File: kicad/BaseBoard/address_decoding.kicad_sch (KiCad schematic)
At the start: 5 parts, among them U5 74LS00, U6 ATF22V10C

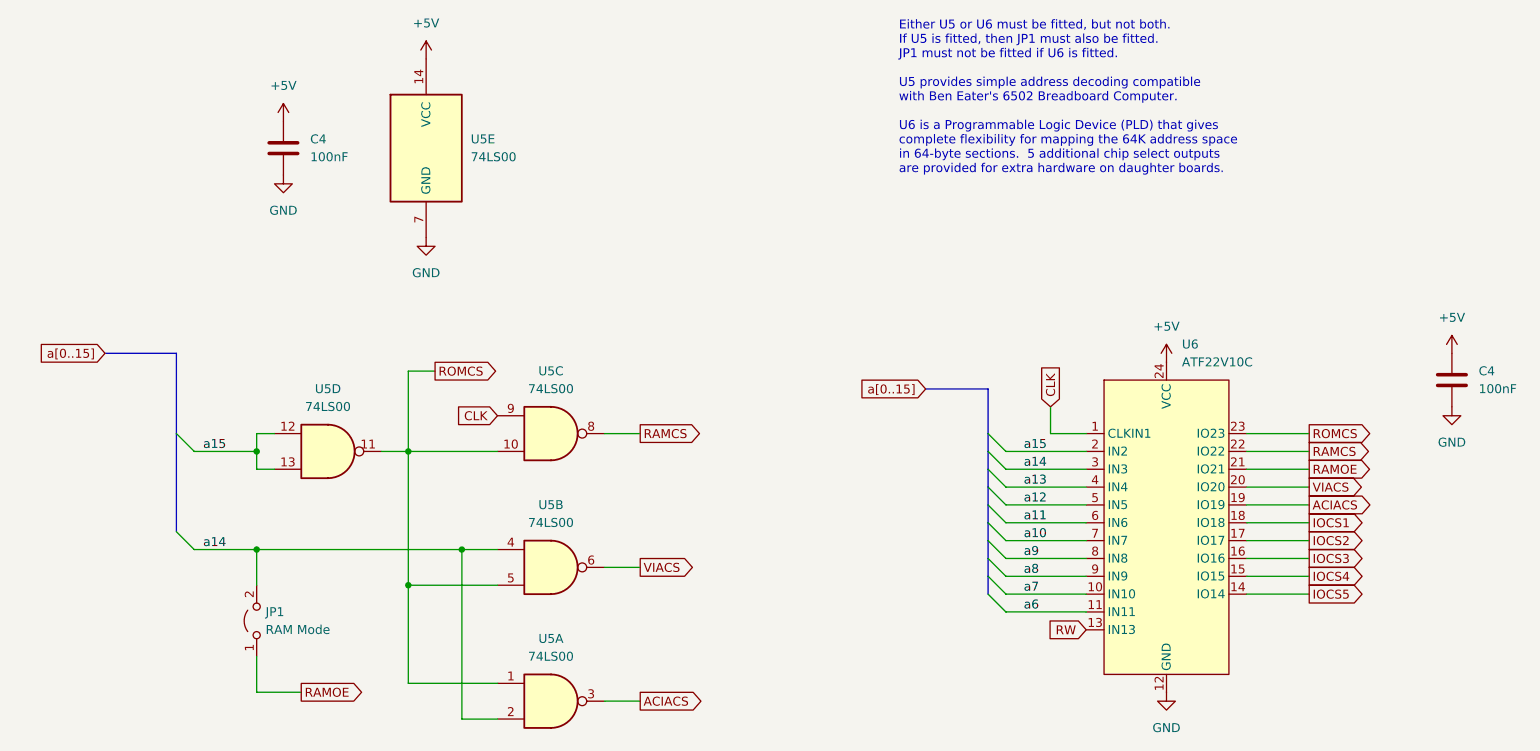
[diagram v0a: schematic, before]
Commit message: I/O board schematic and layout
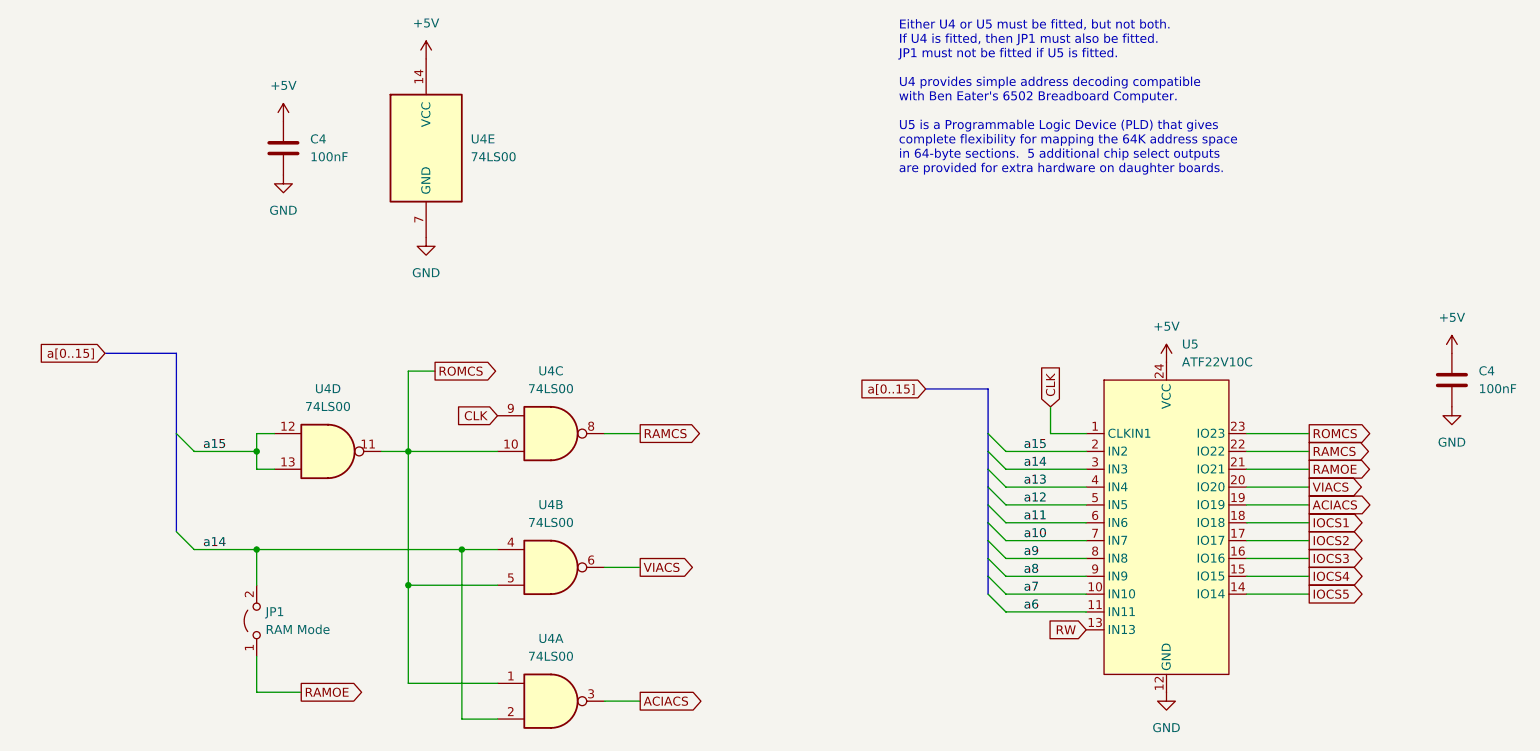
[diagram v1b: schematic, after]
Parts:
- renumbered U5 to U4, U6 to U5
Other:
- note added: "Either U4 or U5 must be fitted, but not both. If U4 is fitted, then JP1 must also be fitted. JP1 must not be fitted if U5 is fitted. U4 provides simple address decoding compatible with Ben Eater's 6502 Breadboard Computer. U5 is a Programmable Logic Device (PLD) that gives complete flexibility for mapping the 64K address space in 64-byte sections. 5 additional chip select outputs are provided for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"
- note removed: "Either U5 or U6 must be fitted, but not both. If U5 is fitted, then JP1 must also be fitted. JP1 must not be fitted if U6 is fitted. U5 provides simple address decoding compatible with Ben Eater's 6502 Breadboard Computer. U6 is a Programmable Logic Device (PLD) that gives complete flexibility for mapping the 64K address space in 64-byte sections. 5 additional chip select outputs are provided for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"
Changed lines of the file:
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@@
     (stroke (width 0) (type default))
   )
-  (text "Either U5 or U6 must be fitted, but not both.\nIf U5 is fitted, then JP1 must also be fitted.\nJP1 must not be fitted if U6 is fitted.\n\nU5 provides simple address decoding compatible\nwith Ben Eater's 6502 Breadboard Computer.\n\nU6 is a Programmable Logic Device (PLD) that gives\ncomplete flexibility for mapping the 64K address space\nin 64-byte sections.  5 additional chip select outputs\nare provided for extra hardware on daughter boards."
+  (text "Either U4 or U5 must be fitted, but not both.\nIf U4 is fitted, then JP1 must also be fitted.\nJP1 must not be fitted if U5 is fitted.\n\nU4 provides simple address decoding compatible\nwith Ben Eater's 6502 Breadboard Computer.\n\nU5 is a Programmable Logic Device (PLD) that gives\ncomplete flexibility for mapping the 64K address space\nin 64-byte sections.  5 additional chip select outputs\nare provided for extra hardware on daughter boards."
     (at 166.37 66.04 0)
     (effects (font (size 1.27 1.27)) (justify left bottom))
@@
         )
         (path "/3f118084-1458-40be-b12b-e8391c9e712b/5996dc94-313e-4b29-a810-4864fe70dd3b"
+          (reference "#PWR034") (unit 1)
+        )
+      )
+    )
+  )
+  (symbol (lib_id "power:GND") (at 99.06 74.93 0) (unit 1)
+    (in_bom yes) (on_board yes) (dnp no) (fields_autoplaced)
+    (property "Reference" "#PWR036" (at 99.06 81.28 0)
+      (effects (font (size 1.27 1.27)) hide)
+    )
+    (property "Value" "GND" (at 99.06 80.01 0)
+      (effects (font (size 1.27 1.27)))
+    )
+    (property "Footprint" "" (at 99.06 74.93 0)
+      (effects (font (size 1.27 1.27)) hide)
+    )
+    (property "Datasheet" "" (at 99.06 74.93 0)
+      (effects (font (size 1.27 1.27)) hide)
+    )
+    (pin "1")
+    (instances
+      (project "MiniComputerBase"
+        (path "/3f118084-1458-40be-b12b-e8391c9e712b/5996dc94-313e-4b29-a810-4864fe70dd3b"
           (reference "#PWR036") (unit 1)
-        )
-      )
-    )
-  )
-  (symbol (lib_id "power:GND") (at 99.06 74.93 0) (unit 1)
-    (in_bom yes) (on_board yes) (dnp no) (fields_autoplaced)
-    (property "Reference" "#PWR038" (at 99.06 81.28 0)
-      (effects (font (size 1.27 1.27)) hide)
-    )
-    (property "Value" "GND" (at 99.06 80.01 0)
-      (effects (font (size 1.27 1.27)))
-    )
-    (property "Footprint" "" (at 99.06 74.93 0)
-      (effects (font (size 1.27 1.27)) hide)
-    )
-    (property "Datasheet" "" (at 99.06 74.93 0)
-      (effects (font (size 1.27 1.27)) hide)
-    )
-    (pin "1")
-    (instances
-      (project "MiniComputerBase"
-        (path "/3f118084-1458-40be-b12b-e8391c9e712b/5996dc94-313e-4b29-a810-4864fe70dd3b"
-          (reference "#PWR038") (unit 1)
         )
       )
@@
   (symbol (lib_id "74xx:74LS00") (at 85.09 105.41 0) (unit 4)
     (in_bom yes) (on_board yes) (dnp no) (fields_autoplaced)
-    (property "Reference" "U5" (at 85.0817 96.52 0)
+    (property "Reference" "U4" (at 85.0817 96.52 0)
       (effects (font (size 1.27 1.27)))
     )
@@
       (project "MiniComputerBase"
         (path "/3f118084-1458-40be-b12b-e8391c9e712b/5996dc94-313e-4b29-a810-4864fe70dd3b"
-          (reference "U5") (unit 4)
+          (reference "U4") (unit 4)
         )
       )
@@
   (symbol (lib_id "74xx:74LS00") (at 116.84 121.92 0) (unit 2)
     (in_bom yes) (on_board yes) (dnp no) (fields_autoplaced)
-    (property "Reference" "U5" (at 116.8317 113.03 0)
+    (property "Reference" "U4" (at 116.8317 113.03 0)
       (effects (font (size 1.27 1.27)))
     )
@@
       (project "MiniComputerBase"
         (path "/3f118084-1458-40be-b12b-e8391c9e712b/5996dc94-313e-4b29-a810-4864fe70dd3b"
-          (reference "U5") (unit 2)
+          (reference "U4") (unit 2)
         )
       )
@@
   (symbol (lib_id "74xx:74LS00") (at 116.84 140.97 0) (unit 1)
     (in_bom yes) (on_board yes) (dnp no) (fields_autoplaced)
-    (property "Reference" "U5" (at 116.8317 132.08 0)
+    (property "Reference" "U4" (at 116.8317 132.08 0)
       (effects (font (size 1.27 1.27)))
     )
@@
       (project "MiniComputerBase"
         (path "/3f118084-1458-40be-b12b-e8391c9e712b/5996dc94-313e-4b29-a810-4864fe70dd3b"
-          (reference "U5") (unit 1)
+          (reference "U4") (unit 1)
         )
       )
@@
   (symbol (lib_id "74xx:74LS00") (at 99.06 62.23 0) (unit 5)
     (in_bom yes) (on_board yes) (dnp no) (fields_autoplaced)
-    (property "Reference" "U5" (at 105.41 60.96 0)
+    (property "Reference" "U4" (at 105.41 60.96 0)
       (effects (font (size 1.27 1.27)) (justify left))
     )
@@
       (project "MiniComputerBase"
         (path "/3f118084-1458-40be-b12b-e8391c9e712b/5996dc94-313e-4b29-a810-4864fe70dd3b"
-          (reference "U5") (unit 5)
+          (reference "U4") (unit 5)
         )
       )
@@
   (symbol (lib_id "74xx:74LS00") (at 116.84 102.87 0) (unit 3)
     (in_bom yes) (on_board yes) (dnp no) (fields_autoplaced)
-    (property "Reference" "U5" (at 116.8317 93.98 0)
+    (property "Reference" "U4" (at 116.8317 93.98 0)
       (effects (font (size 1.27 1.27)))
     )
@@
       (project "MiniComputerBase"
         (path "/3f118084-1458-40be-b12b-e8391c9e712b/5996dc94-313e-4b29-a810-4864fe70dd3b"
-          (reference "U5") (unit 3)
+          (reference "U4") (unit 3)
         )
       )
@@
         )
         (path "/3f118084-1458-40be-b12b-e8391c9e712b/5996dc94-313e-4b29-a810-4864fe70dd3b"
-          (reference "#PWR041") (unit 1)
+          (reference "#PWR039") (unit 1)
         )
       )
@@
   (symbol (lib_id "power:+5V") (at 204.47 92.71 0) (unit 1)
     (in_bom yes) (on_board yes) (dnp no) (fields_autoplaced)
-    (property "Reference" "#PWR039" (at 204.47 96.52 0)
+    (property "Reference" "#PWR037" (at 204.47 96.52 0)
       (effects (font (size 1.27 1.27)) hide)
     )
@@
       (project "MiniComputerBase"
         (path "/3f118084-1458-40be-b12b-e8391c9e712b/5996dc94-313e-4b29-a810-4864fe70dd3b"
-          (reference "#PWR039") (unit 1)
+          (reference "#PWR037") (unit 1)
         )
       )
@@
         )
         (path "/3f118084-1458-40be-b12b-e8391c9e712b/5996dc94-313e-4b29-a810-4864fe70dd3b"
-          (reference "#PWR035") (unit 1)
+          (reference "#PWR033") (unit 1)
         )
       )
@@
         )
         (path "/3f118084-1458-40be-b12b-e8391c9e712b/5996dc94-313e-4b29-a810-4864fe70dd3b"
-          (reference "#PWR042") (unit 1)
+          (reference "#PWR040") (unit 1)
         )
       )
@@
   (symbol (lib_id "power:GND") (at 204.47 139.7 0) (unit 1)
     (in_bom yes) (on_board yes) (dnp no) (fields_autoplaced)
-    (property "Reference" "#PWR040" (at 204.47 146.05 0)
+    (property "Reference" "#PWR038" (at 204.47 146.05 0)
       (effects (font (size 1.27 1.27)) hide)
     )
@@
       (project "MiniComputerBase"
         (path "/3f118084-1458-40be-b12b-e8391c9e712b/5996dc94-313e-4b29-a810-4864fe70dd3b"
-          (reference "#PWR040") (unit 1)
+          (reference "#PWR038") (unit 1)
         )
       )
@@
   (symbol (lib_id "power:+5V") (at 99.06 49.53 0) (unit 1)
     (in_bom yes) (on_board yes) (dnp no) (fields_autoplaced)
-    (property "Reference" "#PWR037" (at 99.06 53.34 0)
+    (property "Reference" "#PWR035" (at 99.06 53.34 0)
       (effects (font (size 1.27 1.27)) hide)
     )
@@
       (project "MiniComputerBase"
         (path "/3f118084-1458-40be-b12b-e8391c9e712b/5996dc94-313e-4b29-a810-4864fe70dd3b"
-          (reference "#PWR037") (unit 1)
+          (reference "#PWR035") (unit 1)
         )
       )
@@
   (symbol (lib_id "ATF22V10C:ATF22V10C") (at 204.47 90.17 0) (unit 1)
     (in_bom yes) (on_board yes) (dnp no) (fields_autoplaced)
-    (property "Reference" "U6" (at 206.6641 90.17 0)
+    (property "Reference" "U5" (at 206.6641 90.17 0)
       (effects (font (size 1.27 1.27)) (justify left))
     )
@@
       (project "MiniComputerBase"
         (path "/3f118084-1458-40be-b12b-e8391c9e712b/5996dc94-313e-4b29-a810-4864fe70dd3b"
-          (reference "U6") (unit 1)
-        )
-      )
+          (reference "U5") (unit 1)
+        )
+      )
